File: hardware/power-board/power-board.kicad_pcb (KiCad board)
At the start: 2 copper layers, 193 x 65 mm, 33 parts, among them J1 SW_SPST, J2 Main Board, J3 DMX512 Out Jack, J4 DMX512, K1 SPST-NO, K2 SPST-NO, P1 IEC320-C14, P2 IEC320-C13, P3 IEC320-C13, U1 SZNUD3124DMT1G, U2 THVD1439

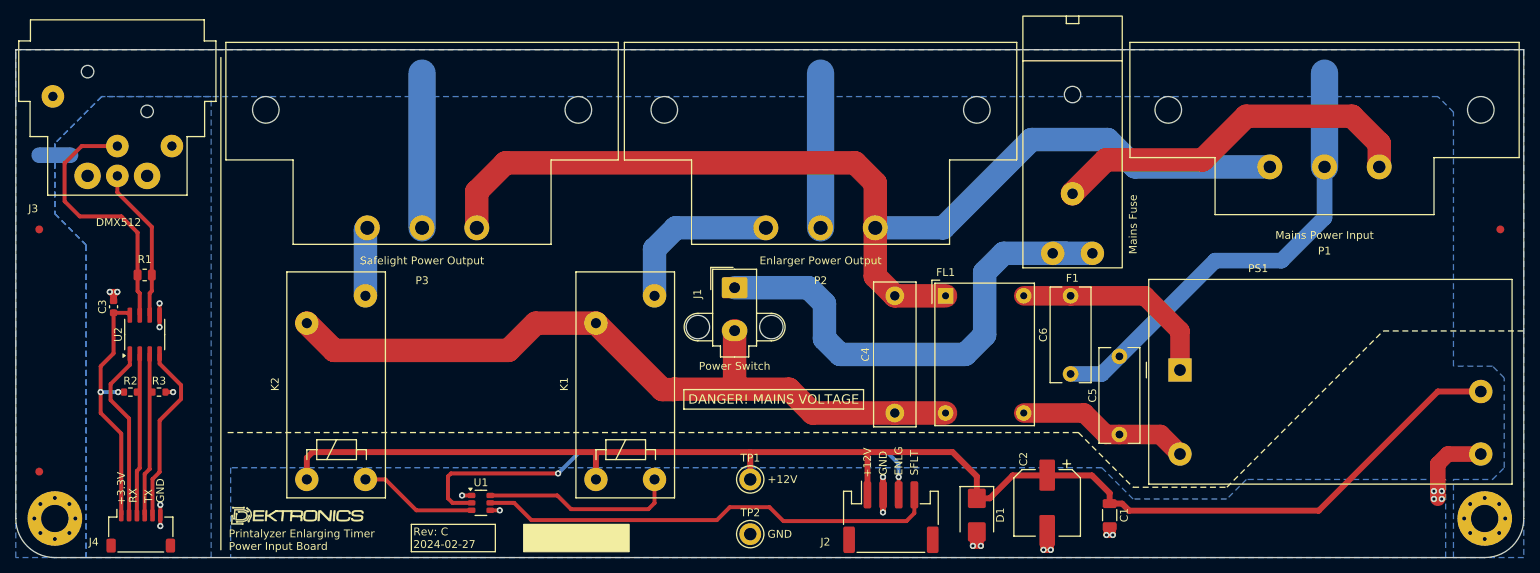
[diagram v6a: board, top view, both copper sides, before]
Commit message: Numerous updates and tweaks to power board EMI filter addition
Refs #56

Swapped all of the main filter components with slightly smaller
versions, to help with clearance for main power traces.
Added a UL1676 recognized resistor to act as a bleeder for the X
capacitor.

Arranged traces to keep at least 3mm clearance between all mains AC
traces, and >4mm clearance between any mains AC trace and the DC side.
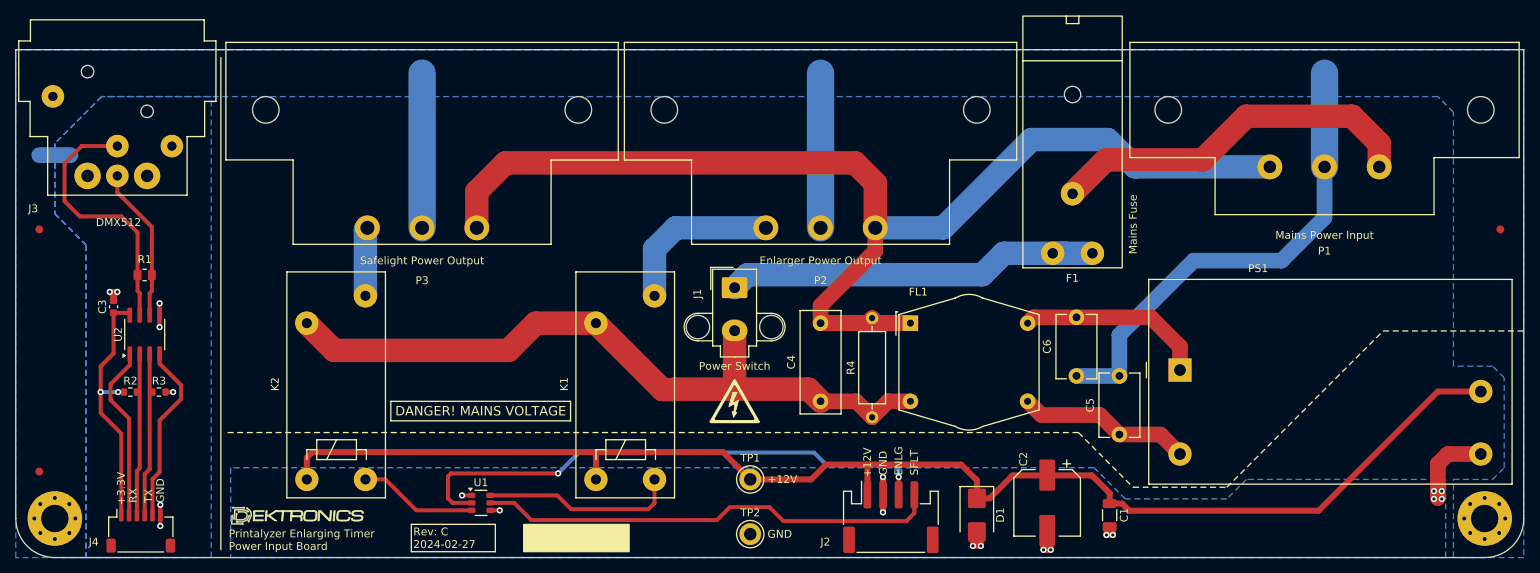
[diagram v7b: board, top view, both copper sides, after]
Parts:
- added R4: 1M(1/2W), Resistor_THT:R_Axial_DIN0309_L9.0mm_D3.2mm_P12.70mm_Horizontal, F.Cu at (145.6, 87.0)
- added REF**: Symbol_HighVoltage_Triangle_6x6mm_SilkScreen, lib_fp:Symbol_HighVoltage_Triangle_6x6mm_SilkScreen, F.Cu at (128.0, 85.0)
- C4: footprint lib_fp:C_Rect_L18.0mm_W5.0mm_P15.00mm_Kemet_R46 -> lib_fp:C_Rect_L13.0mm_W5.0mm_P10.00mm_Kemet_R46
- C5, C6: value 2200pF(Y1) -> 2200pF(Y2); footprint lib_fp:C_Disc_D12.0mm_W5.0mm_P10.00mm_Vishay_VY1 -> lib_fp:C_Disc_D8.0mm_W5.0mm_P7.50mm_Vishay_VY2
- FL1: footprint lib_fp:Choke_Schaffner_RN212-02-12.5x18.0mm -> lib_fp:Choke_Schaffner_RN112-02-17.7x17.1mm
- moved C4 9.62 mm to (139.0, 85.0)
- moved FL1 5.70 mm to (150.5, 75.0)
- moved C6 0.79 mm to (171.8, 81.8)
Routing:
- net NEUT: track 136.8 -> 159.2 mm
- net Net-(J1-A): track 63.8 -> 49.4 mm
- net +12V: track 180.5 -> 176.6 mm
- net LINE: track 96.9 -> 93.5 mm
- net /AC_F_N: track 26.9 -> 24.4 mm
- net Earth: track 98.9 -> 101.3 mm
